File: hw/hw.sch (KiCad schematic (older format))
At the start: 8 parts

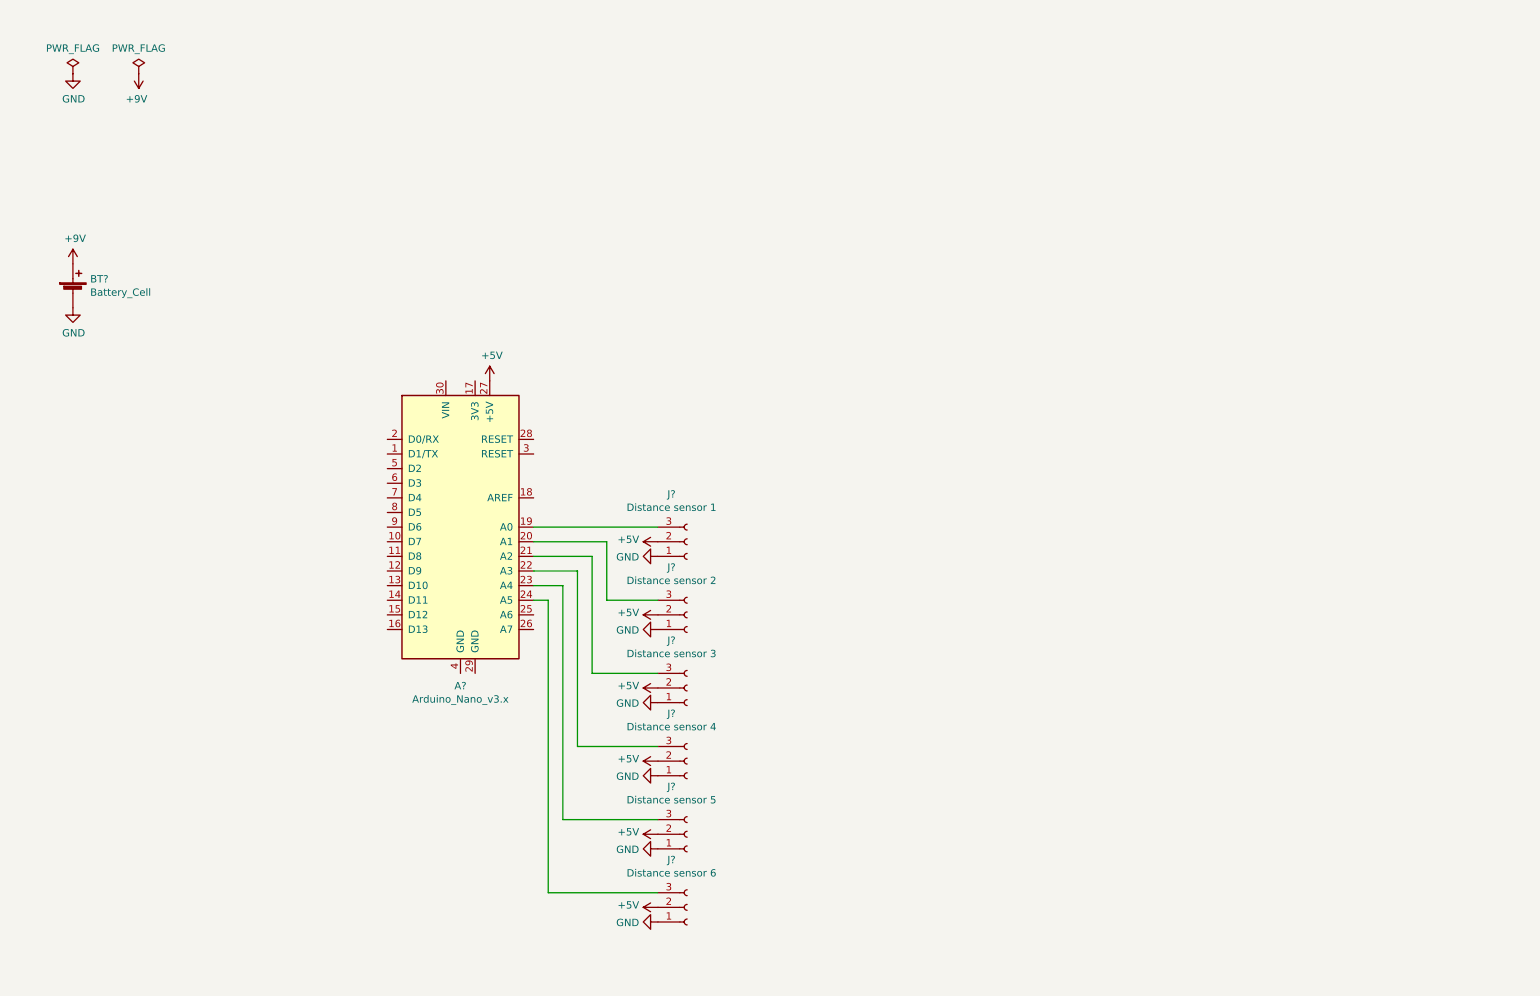
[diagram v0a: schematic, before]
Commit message: Added resistors for distance sensors. Added motor driver and shift register for more output
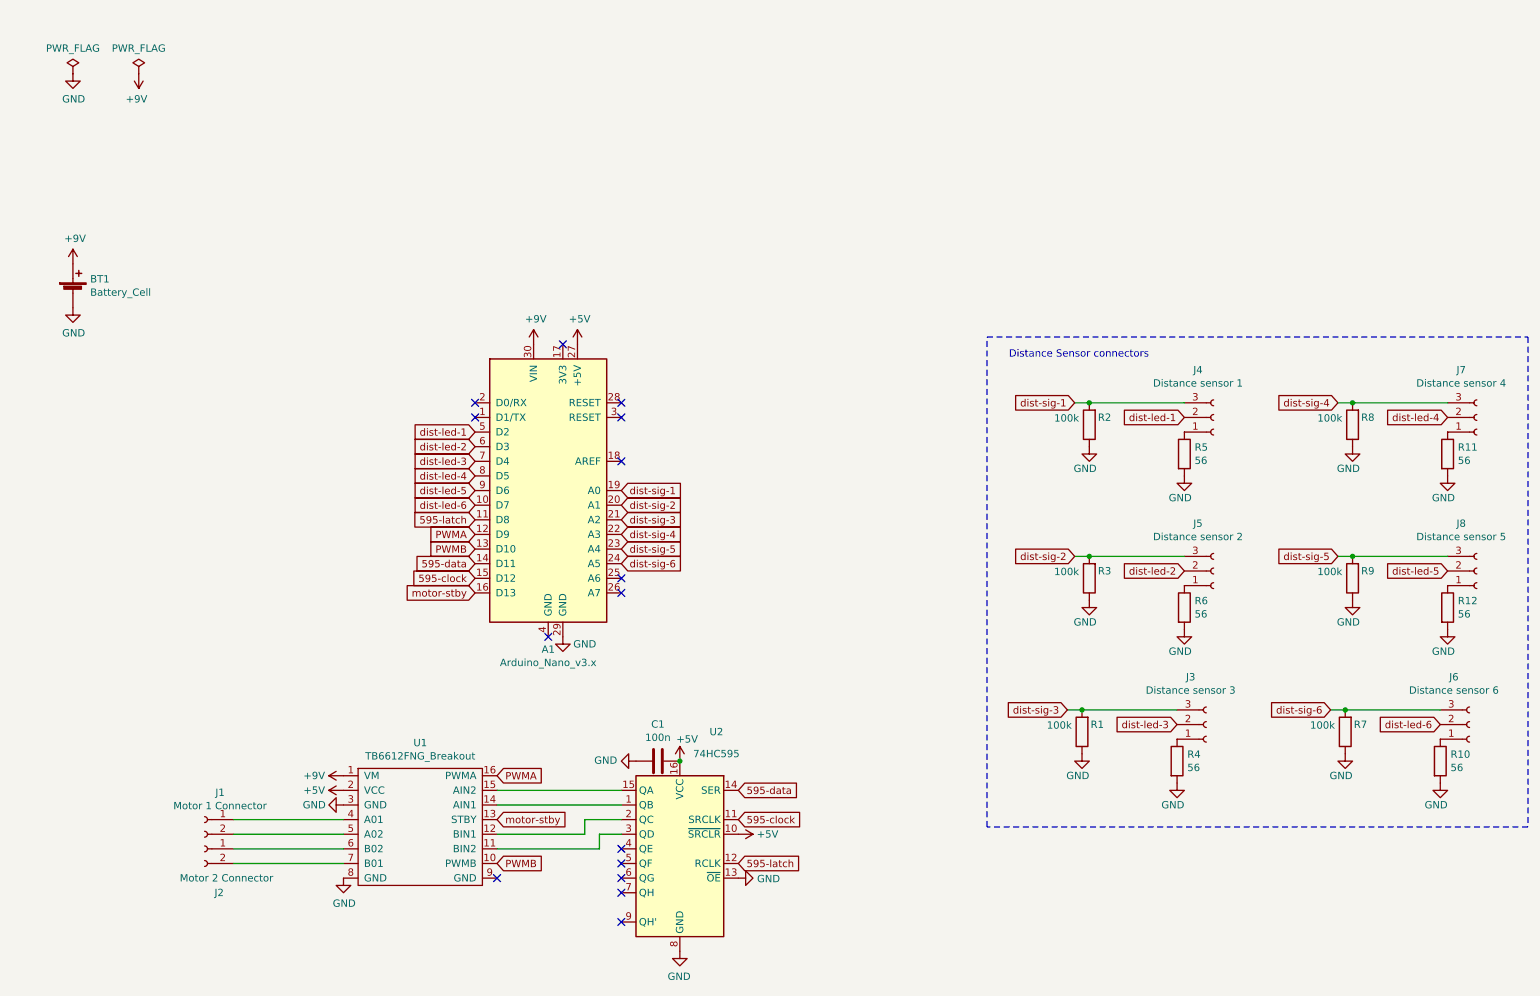
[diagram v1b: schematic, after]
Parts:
- removed J?: Distance sensor 2, symbol Connector:Conn_01x03_Female
- removed J?: Distance sensor 3, symbol Connector:Conn_01x03_Female
- removed J?: Distance sensor 4, symbol Connector:Conn_01x03_Female
- removed J?: Distance sensor 5, symbol Connector:Conn_01x03_Female
- removed J?: Distance sensor 6, symbol Connector:Conn_01x03_Female
- added C1: 100n, Capacitor_THT:C_Disc_D4.7mm_W2.5mm_P5.00mm, symbol Device:C
- added J1: Motor 1 Connector, Connector_PinSocket_2.54mm:PinSocket_1x02_P2.54mm_Vertical, symbol Connector:Conn_01x02_Female
- added J2: Motor 2 Connector, Connector_PinSocket_2.54mm:PinSocket_1x02_P2.54mm_Vertical, symbol Connector:Conn_01x02_Female
- added J3: Distance sensor 3, Connector_PinSocket_2.54mm:PinSocket_1x03_P2.54mm_Vertical, symbol Connector:Conn_01x03_Female
- added J5: Distance sensor 2, Connector_PinSocket_2.54mm:PinSocket_1x03_P2.54mm_Vertical, symbol Connector:Conn_01x03_Female
- added J6: Distance sensor 6, Connector_PinSocket_2.54mm:PinSocket_1x03_P2.54mm_Vertical, symbol Connector:Conn_01x03_Female
- added J7: Distance sensor 4, Connector_PinSocket_2.54mm:PinSocket_1x03_P2.54mm_Vertical, symbol Connector:Conn_01x03_Female
- added J8: Distance sensor 5, Connector_PinSocket_2.54mm:PinSocket_1x03_P2.54mm_Vertical, symbol Connector:Conn_01x03_Female
- added R1, R2, R3, R7, R8, R9: 100k, Resistor_THT:R_Axial_DIN0207_L6.3mm_D2.5mm_P7.62mm_Horizontal, symbol Device:R
- added R10, R11, R12, R4, R5, R6: 56, Resistor_THT:R_Axial_DIN0207_L6.3mm_D2.5mm_P7.62mm_Horizontal, symbol Device:R
- added U1: TB6612FNG_Breakout, symbol custom:TB6612FNG_Breakout
- added U2: 74HC595, Package_DIP:DIP-16_W7.62mm_Socket_LongPads, symbol 74xx:74HC595
- BT1: renamed from BT?; footprint (none) -> Connector_PinSocket_2.54mm:PinSocket_1x02_P2.54mm_Vertical
- J4: renamed from J?; footprint (none) -> Connector_PinSocket_2.54mm:PinSocket_1x03_P2.54mm_Vertical
- gave numbers to parts that had none: 1
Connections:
- net +5V: now also C1.2, U1.2 (VCC), U2.10 (~SRCLR), U2.16 (VCC); no longer J4.2 (Pin_2)
- net +9V: now also A1.30 (VIN), U1.1 (VM)
- net GND: now also A1.29 (GND), C1.1, R1.1, R10.2, R11.2, R12.2, R2.1, R3.1, R4.2, R5.2, R6.2, R7.1, R8.1, R9.1, U1.3 (GND), U1.8 (GND), U2.13 (~OE), U2.8 (GND); no longer J4.1 (Pin_1)
- net dist-led-6: now reaches A1.10 (D7)
- net dist-led-6: now also J6.2 (Pin_2)
- net 595-latch: now reaches A1.11 (D8)
- net 595-latch: now also U2.12 (RCLK)
- net PWMA: now reaches A1.12 (D9)
- net PWMA: now also U1.16 (PWMA)
- net PWMB: now reaches A1.13 (D10)
- net PWMB: now also U1.10 (PWMB)
- net 595-data: now reaches A1.14 (D11)
- net 595-data: now also U2.14 (SER)
- net 595-clock: now reaches A1.15 (D12)
- net 595-clock: now also U2.11 (SRCLK)
- net motor-stby: now reaches A1.16 (D13)
- net motor-stby: now also U1.13 (STBY)
- net dist-sig-1: now reaches A1.19 (A0), J4.3 (Pin_3)
- net dist-sig-1: now also R2.2
- net dist-sig-2: now reaches A1.20 (A1)
- net dist-sig-2: now also J5.3 (Pin_3), R3.2
- net dist-sig-3: now reaches A1.21 (A2)
- net dist-sig-3: now also J3.3 (Pin_3), R1.2
- net dist-sig-4: now reaches A1.22 (A3)
- net dist-sig-4: now also J7.3 (Pin_3), R8.2
- net dist-sig-5: now reaches A1.23 (A4)
- net dist-sig-5: now also J8.3 (Pin_3), R9.2
- net dist-sig-6: now reaches A1.24 (A5)
- net dist-sig-6: now also J6.3 (Pin_3), R7.2
- net dist-led-1: now reaches A1.5 (D2)
- net dist-led-1: now also J4.2 (Pin_2)
- net dist-led-2: now reaches A1.6 (D3)
- net dist-led-2: now also J5.2 (Pin_2)
- net dist-led-3: now reaches A1.7 (D4)
- net dist-led-3: now also J3.2 (Pin_2)
- net dist-led-4: now reaches A1.8 (D5)
- net dist-led-4: now also J7.2 (Pin_2)
- net dist-led-5: now reaches A1.9 (D6)
- net dist-led-5: now also J8.2 (Pin_2)
- new net: J4.1 (Pin_1), R5.1
- new net: J5.1 (Pin_1), R6.1
- new net: U1.11 (BIN2), U2.3 (QD)
- new net: U1.12 (BIN1), U2.2 (QC)
- new net: U1.14 (AIN1), U2.1 (QB)
- new net: U1.15 (AIN2), U2.15 (QA)
- new net: J1.1 (Pin_1), U1.4 (A01)
- new net: J1.2 (Pin_2), U1.5 (A02)
- new net: J2.1 (Pin_1), U1.6 (B02)
- new net: J2.2 (Pin_2), U1.7 (B01)
- new net: J3.1 (Pin_1), R4.1
- new net: J7.1 (Pin_1), R11.1
- new net: J8.1 (Pin_1), R12.1
- new net: J6.1 (Pin_1), R10.1
- no-connect marks 0 -> 15
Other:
- note added: "Distance Sensor connectors"
- moved on the sheet: A1, J4

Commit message: Saved schematic file
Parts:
- U1: footprint (none) -> custom:TB6612FNG breakout
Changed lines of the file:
@@
 F 0 "U1" H 3325 5775 50  0000 C CNN
 F 1 "TB6612FNG_Breakout" H 3325 5684 50  0000 C CNN
-F 2 "" H 3300 5650 50  0001 C CNN
+F 2 "custom:TB6612FNG breakout" H 3300 5650 50  0001 C CNN
 F 3 "" H 3300 5650 50  0001 C CNN
 	1    3300 5650

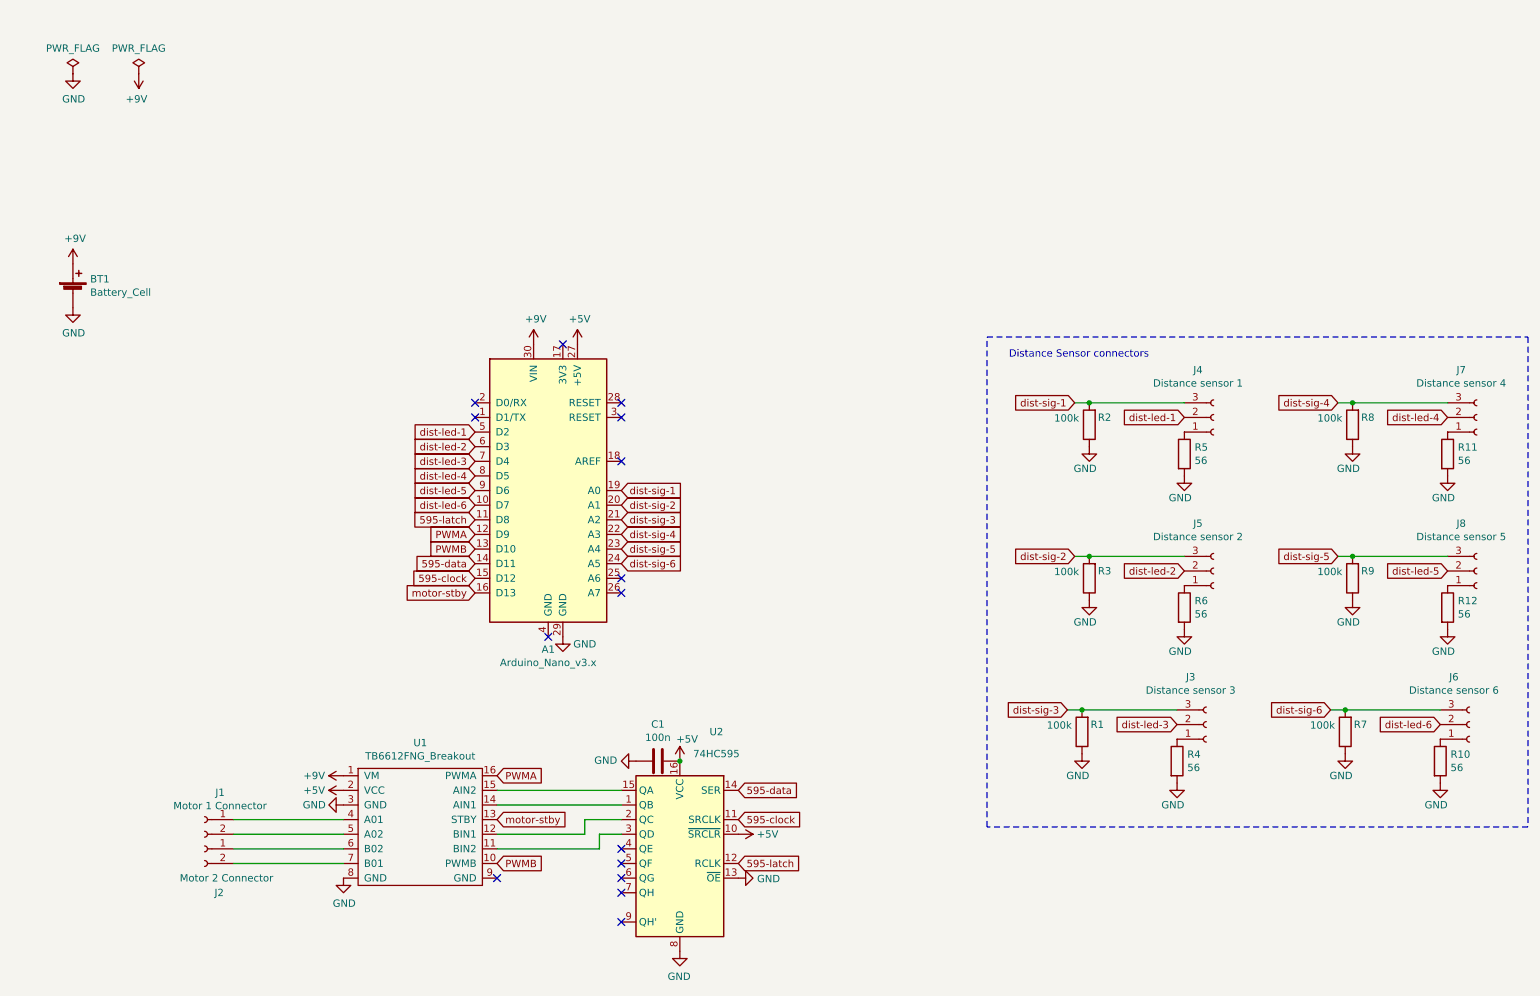
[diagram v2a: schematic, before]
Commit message: Laid out PCB footprints
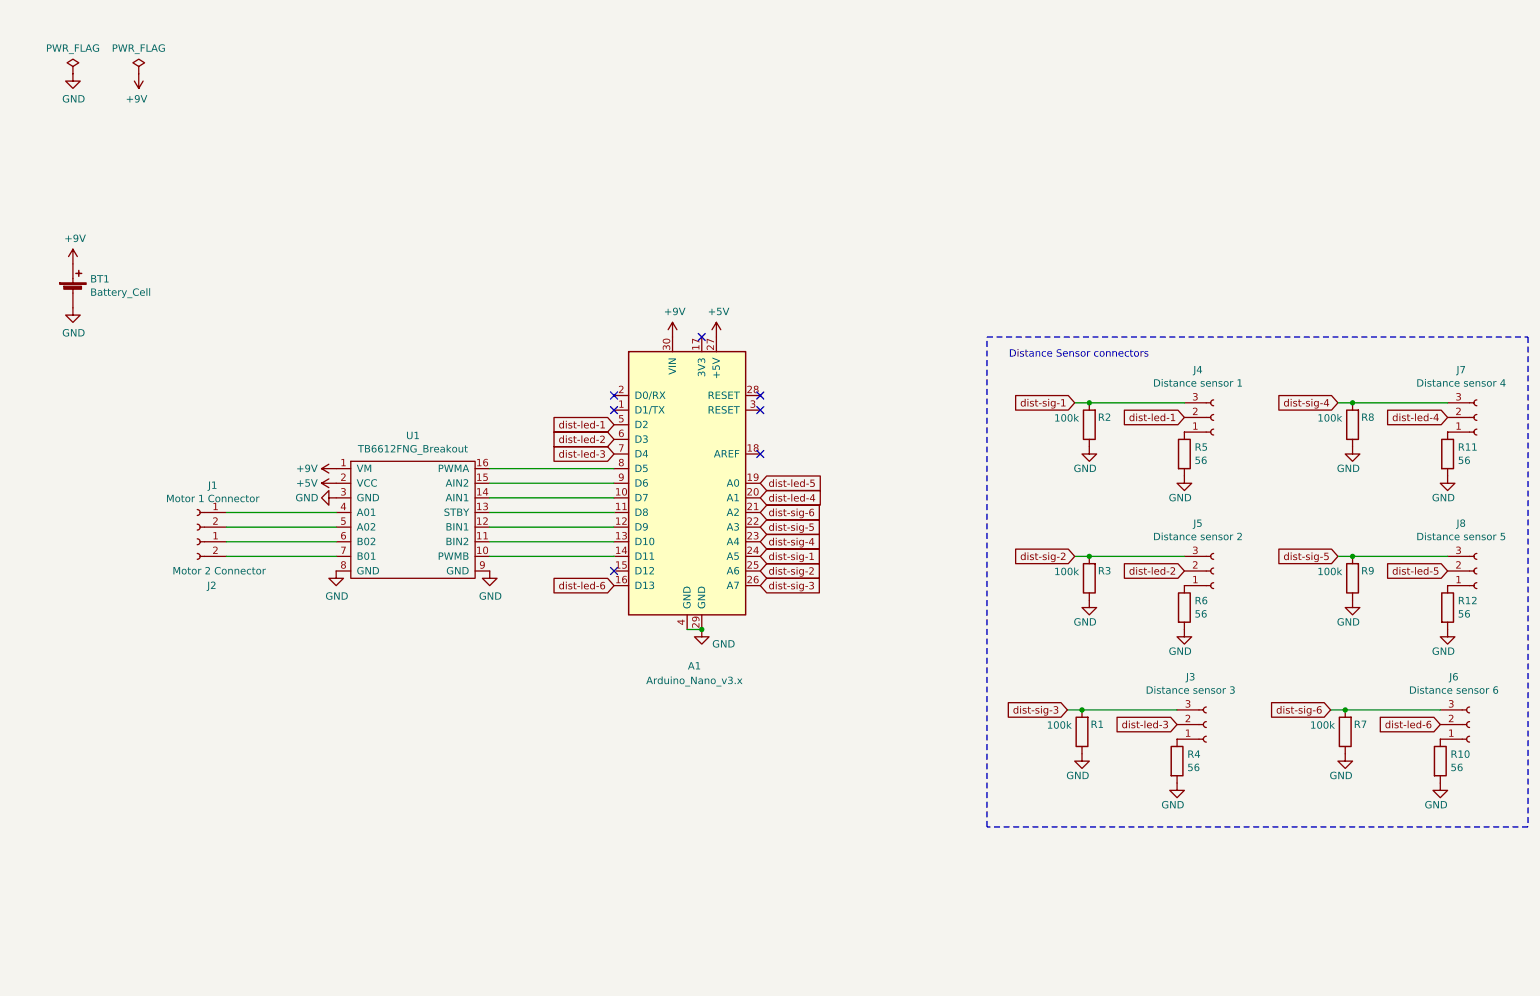
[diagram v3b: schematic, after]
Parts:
- removed C1: 100n, Capacitor_THT:C_Disc_D4.7mm_W2.5mm_P5.00mm, symbol Device:C
- removed U2: 74HC595, Package_DIP:DIP-16_W7.62mm_Socket_LongPads, symbol 74xx:74HC595
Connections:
- net GND: now also A1.4 (GND), U1.9 (GND)
- net dist-led-4: now also A1.20 (A1); no longer A1.8 (D5)
- net dist-led-5: now also A1.19 (A0); no longer A1.9 (D6)
- net dist-led-6: now also A1.16 (D13); no longer A1.10 (D7)
- net dist-sig-1: now also A1.24 (A5); no longer A1.19 (A0)
- net dist-sig-2: now also A1.25 (A6); no longer A1.20 (A1)
- net dist-sig-3: now also A1.26 (A7); no longer A1.21 (A2)
- net dist-sig-4: now also A1.23 (A4); no longer A1.22 (A3)
- net dist-sig-5: now also A1.22 (A3); no longer A1.23 (A4)
- net dist-sig-6: now also A1.21 (A2); no longer A1.24 (A5)
- net at U1.11 (BIN2): now also A1.13 (D10)
- net at U1.12 (BIN1): now also A1.12 (D9)
- net at U1.14 (AIN1): now also A1.10 (D7)
- net at U1.15 (AIN2): now also A1.9 (D6)
- net 595-clock: no longer names the net of A1.15 (D12)
- net 595-data: no longer names the net of A1.14 (D11)
- net 595-data: now also U1.10 (PWMB)
- net 595-latch: no longer names the net of A1.11 (D8)
- net 595-latch: now also U1.13 (STBY)
- net PWMA: no longer names the net of U1.16 (PWMA)
- net PWMA: now also A1.8 (D5); no longer A1.12 (D9)
- removed net PWMB: A1.13 (D10), U1.10 (PWMB)
- removed net motor-stby: A1.16 (D13), U1.13 (STBY)
- no-connect marks 15 -> 7
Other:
- moved on the sheet: A1, J1, J2, U1

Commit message: new pcb version
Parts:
- removed J6: Distance sensor 6, Connector_PinSocket_2.54mm:PinSocket_1x03_P2.54mm_Vertical, symbol Connector:Conn_01x03_Female
- removed R11, R12: 56, Resistor_THT:R_Axial_DIN0207_L6.3mm_D2.5mm_P7.62mm_Horizontal, symbol Device:R
- added C1: 100u, Capacitor_THT:CP_Radial_D6.3mm_P2.50mm, symbol Device:CP
- added C2, C3, C4, C5, C6, C7: 100n, Capacitor_SMD:C_0805_2012Metric_Pad1.15x1.40mm_HandSolder, symbol Device:C
- added D1: 1N5817, Diode_THT:D_DO-41_SOD81_P7.62mm_Horizontal, symbol Device:D
- added J6: Serial pin header, Connector_PinHeader_2.54mm:PinHeader_1x02_P2.54mm_Vertical, symbol Connector:Conn_01x02_Male
- added U2: L3GD20_breakout, custom:L3GD20_breakout, symbol custom:L3GD20_breakout
- J3: value Distance sensor 3 -> Distance sensor 2
- J5: value Distance sensor 2 -> Distance sensor 3
- R1, R2, R3, R7, R9: value 100k -> 1M; footprint Resistor_THT:R_Axial_DIN0207_L6.3mm_D2.5mm_P7.62mm_Horizontal -> Resistor_SMD:R_0805_2012Metric_Pad1.15x1.40mm_HandSolder
- R10, R4, R5, R6: value 56 -> 330; footprint Resistor_THT:R_Axial_DIN0207_L6.3mm_D2.5mm_P7.62mm_Horizontal -> Resistor_SMD:R_0805_2012Metric_Pad1.15x1.40mm_HandSolder
- R8: value 100k -> 330; footprint Resistor_THT:R_Axial_DIN0207_L6.3mm_D2.5mm_P7.62mm_Horizontal -> Resistor_SMD:R_0805_2012Metric_Pad1.15x1.40mm_HandSolder
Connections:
- net dist-led-6 is gone; now on net dist-led-5: A1.16 (D13)
- net +5V: now also U2.1 (Vin)
- net +9V: now also D1.2 (A); no longer A1.30 (VIN)
- net GND: now also R8.2, C1.2, C2.2, C3.2, C4.2, C5.2, C6.2, C7.2, U2.3 (GND); no longer R8.1
- net dist-led-2: now also J3.2 (Pin_2); no longer J5.2 (Pin_2)
- net dist-led-3: now also J5.2 (Pin_2); no longer J3.2 (Pin_2)
- net dist-led-4: now also A1.15 (D12); no longer A1.20 (A1)
- net dist-led-5: no longer A1.19 (A0)
- net dist-sig-1: now also A1.19 (A0), C3.1; no longer A1.24 (A5)
- net dist-sig-2: now also A1.20 (A1), J3.3 (Pin_3), R1.2, C4.1; no longer A1.25 (A6), J5.3 (Pin_3), R3.2
- net dist-sig-3: now also A1.21 (A2), J5.3 (Pin_3), R3.2, C5.1; no longer A1.26 (A7), J3.3 (Pin_3), R1.2
- net dist-sig-4: now also A1.25 (A6), R7.2, C6.1; no longer A1.23 (A4), R8.2
- net dist-sig-5: now also A1.26 (A7), C7.1; no longer A1.22 (A3)
- net at A1.1 (D1/TX): now also J6.2 (Pin_2)
- net at A1.2 (D0/RX): now also J6.1 (Pin_1)
- net at J7.1 (Pin_1): now also R8.1
- net at J8.1 (Pin_1): now also R10.1
- removed net dist-sig-6: A1.21 (A2), R7.2
- new net IMU_SCL: A1.24 (A5), U2.4 (SCL)
- new net IMU_SDA: A1.23 (A4), U2.5 (SDA)
- new net V_a: A1.30 (VIN), C1.1, C2.1, D1.1 (K)
- no-connect marks 7 -> 11
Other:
- note added: "Polarity protection"
- moved on the sheet: BT1, J4, R2, R5
